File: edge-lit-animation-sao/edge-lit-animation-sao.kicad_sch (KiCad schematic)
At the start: 70 parts, among them J1 USB_C_Receptacle_USB2.0_16P, J3 Conn_02x03_Odd_Even, SW1 SW_Push, SW2 SW_Push, SW3 SW_Push, SW4 SW_Push, U1 RP2040, U2 W25Q128JVS, U3 XC6206PxxxMR, U4 PAM8301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

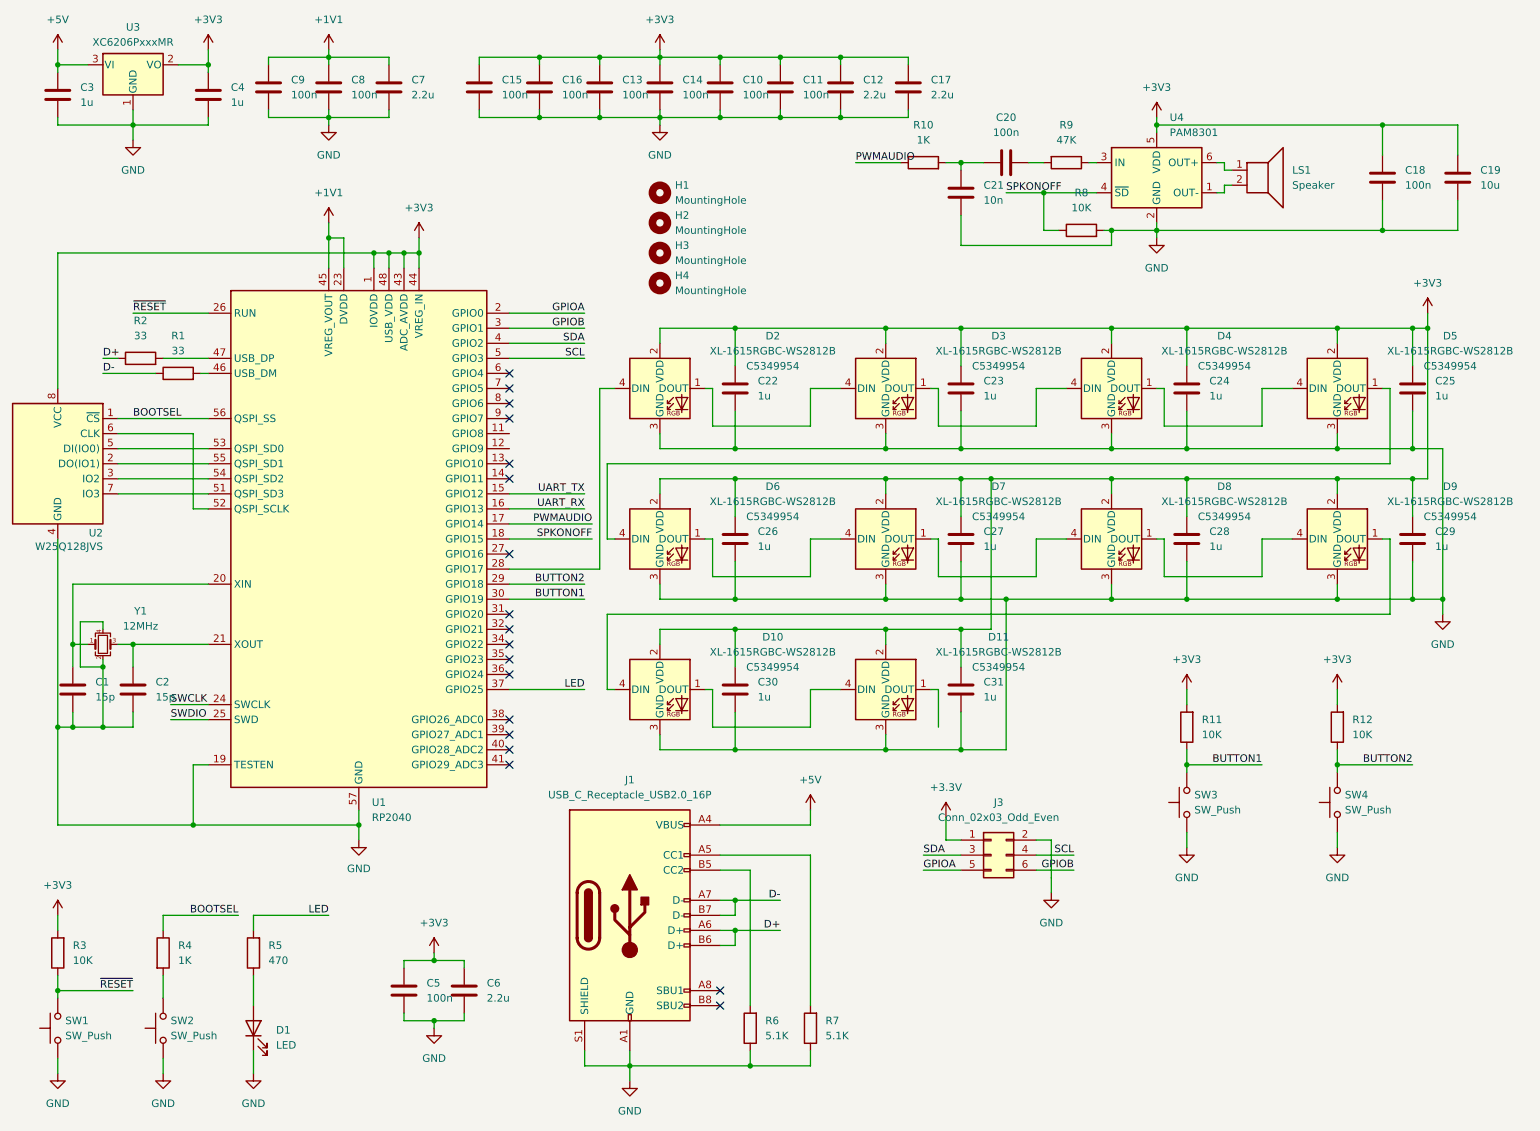
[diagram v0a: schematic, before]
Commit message: Changing from WS2812s to standard white LEDs
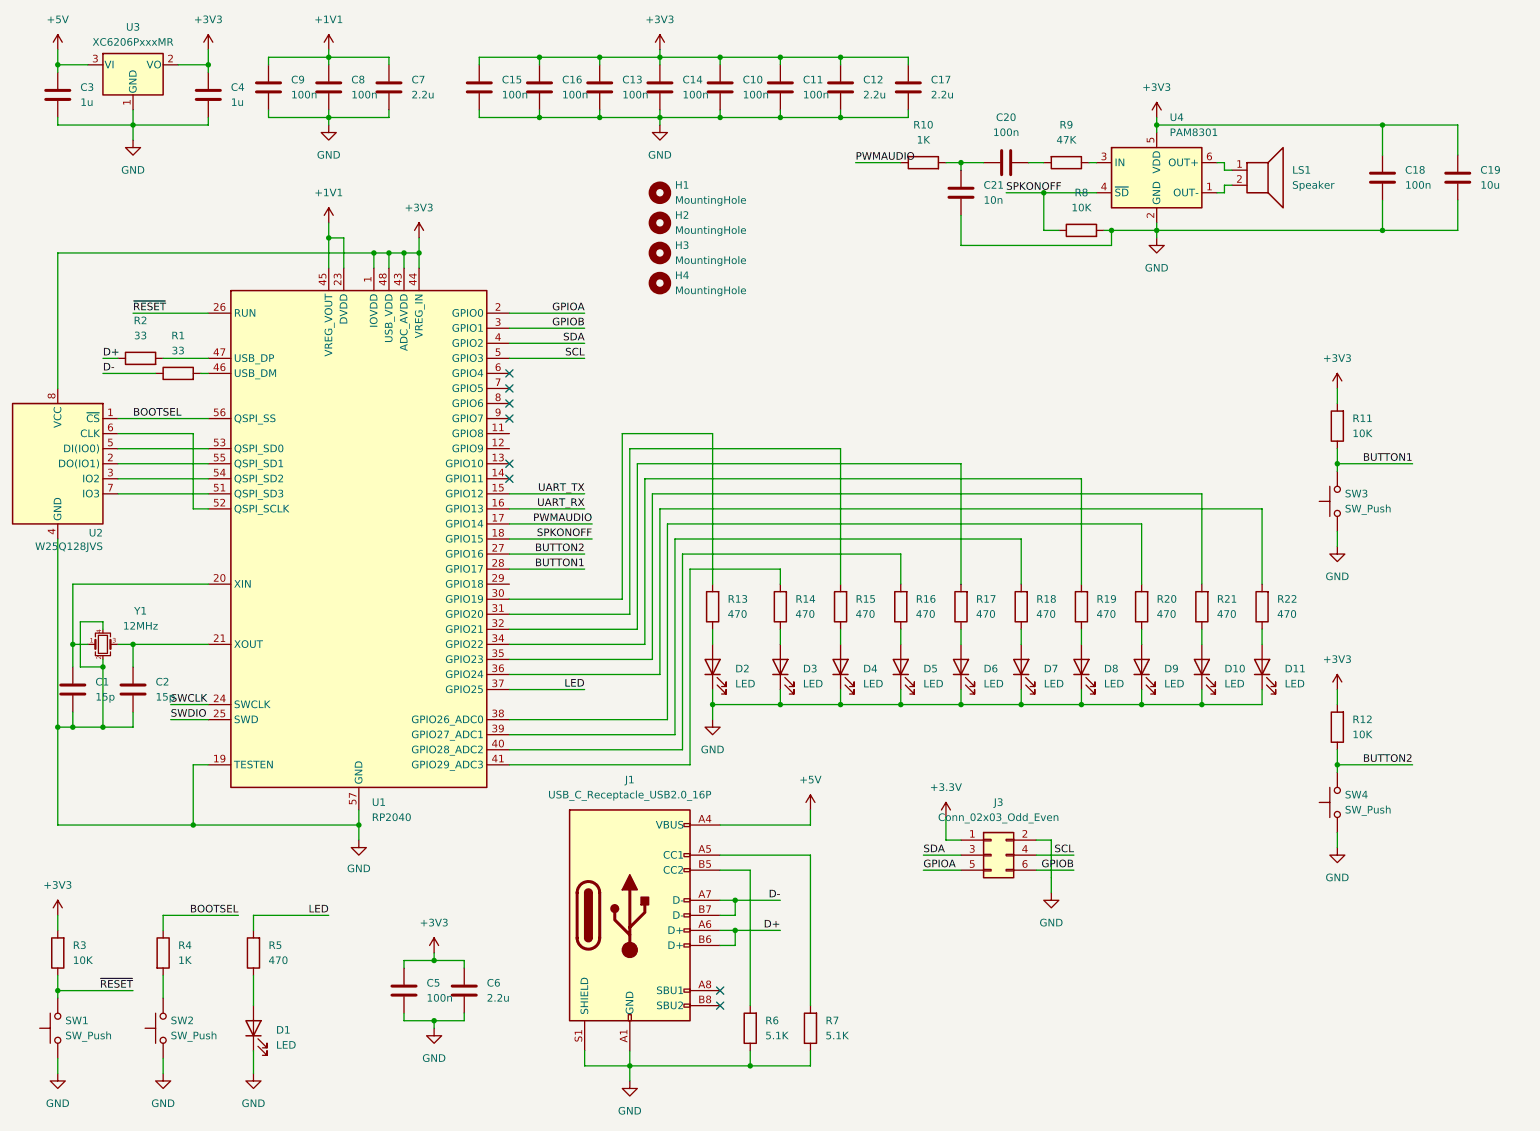
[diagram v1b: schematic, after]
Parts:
- removed C22, C23, C24, C25, C26, C27, C28, C29, C30, C31: 1u, Capacitor_SMD:C_0402_1005Metric, symbol Device:C
- removed D10, D11, D2, D3, D4, D5, D6, D7, D8, D9: XL-1615RGBC-WS2812B, edge-lit-parts:LED-SMD_4P-L1.6-W1.5_XL-1615RGBC-WS2812B, symbol homebrew:XINGLIGHT-XL-1615RGBC-WS2812B
- added D10, D11, D2, D3, D4, D5, D6, D7, D8, D9: LED, LED_SMD:LED_0805_2012Metric_Pad1.15x1.40mm_HandSolder, symbol Device:LED
- added R13, R14, R15, R16, R17, R18, R19, R20, R21, R22: 470, Resistor_SMD:R_0402_1005Metric, symbol Device:R
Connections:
- net BUTTON1: now also U1.28 (GPIO17); no longer U1.30 (GPIO19)
- net BUTTON2: now also U1.27 (GPIO16); no longer U1.29 (GPIO18)
- net GND: now also D10.1 (K), D11.1 (K), D2.1 (K), D3.1 (K), D4.1 (K), D5.1 (K), D6.1 (K), D7.1 (K), D8.1 (K), D9.1 (K)
- net at U1.31 (GPIO20): now also R15.2
- net at U1.32 (GPIO21): now also R17.2
- net at U1.34 (GPIO22): now also R19.2
- net at U1.35 (GPIO23): now also R21.2
- net at U1.36 (GPIO24): now also R22.2
- net at U1.38 (GPIO26_ADC0): now also R20.2
- net at U1.39 (GPIO27_ADC1): now also R18.2
- net at U1.40 (GPIO28_ADC2): now also R16.2
- net at U1.41 (GPIO29_ADC3): now also R14.2
- new net: D4.2 (A), R15.1
- new net: D11.2 (A), R22.1
- new net: D2.2 (A), R13.1
- new net: R13.2, U1.30 (GPIO19)
- new net: D6.2 (A), R17.1
- new net: D7.2 (A), R18.1
- new net: D10.2 (A), R21.1
- new net: D8.2 (A), R19.1
- new net: D3.2 (A), R14.1
- new net: D9.2 (A), R20.1
- new net: D5.2 (A), R16.1
- no-connect marks 18 -> 8
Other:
- moved on the sheet: R11, SW3
